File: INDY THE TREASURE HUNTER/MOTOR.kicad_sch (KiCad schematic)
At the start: 0 parts

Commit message: .
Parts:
- added M?: Motor_DC, symbol Motor:Motor_DC
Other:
- note added: "Driver"
- note added: "Motor"
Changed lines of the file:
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@@
 (kicad_sch (version 20230121) (generator eeschema)
   (paper "A4")
+  (rectangle (start 74.93 60.96) (end 105.41 90.17)
+    (stroke (width 0) (type default))
+    (fill (type none))
+  )
+  (rectangle (start 149.86 59.69) (end 196.85 95.25)
+    (stroke (width 0) (type default))
+    (fill (type none))
+  )
+  (text "Driver\n" (at 87.63 59.69 0)
+    (effects (font (size 1.27 1.27)) (justify left bottom))
+  )
+  (text "Motor\n" (at 168.91 57.15 0)
+    (effects (font (size 1.27 1.27)) (justify left bottom))
+  )
+  (symbol (lib_id "Motor:Motor_DC") (at 172.72 73.66 0) (unit 1)
+    (in_bom yes) (on_board yes) (dnp no) (fields_autoplaced)
+    (property "Reference" "M?" (at 177.8 75.565 0)
+      (effects (font (size 1.27 1.27)) (justify left))
+    )
+    (property "Value" "Motor_DC" (at 177.8 78.105 0)
+      (effects (font (size 1.27 1.27)) (justify left))
+    )
+    (property "Footprint" "" (at 172.72 75.946 0)
+      (effects (font (size 1.27 1.27)) hide)
+    )
+    (property "Datasheet" "~" (at 172.72 75.946 0)
+      (effects (font (size 1.27 1.27)) hide)
+    )
+    (pin "1")
+    (pin "2")
+    (instances
+      (project "INDY THE TREASURE HUNTER"
+        (path "/b3b90d4c-73f4-4a78-9e6e-dd19a1913646/0010784b-0c24-451a-8397-89ffe2babef6"
+          (reference "M?") (unit 1)
+        )
+      )
+    )
+  )
 )

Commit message: 17:32
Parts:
- gave numbers to parts that had none: 1
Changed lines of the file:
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@@
   (symbol (lib_id "Motor:Motor_DC") (at 172.72 73.66 0) (unit 1)
     (in_bom yes) (on_board yes) (dnp no) (fields_autoplaced)
-    (property "Reference" "M?" (at 177.8 75.565 0)
+    (property "Reference" "M1" (at 177.8 75.565 0)
       (effects (font (size 1.27 1.27)) (justify left))
     )
@@
       (project "INDY THE TREASURE HUNTER"
         (path "/b3b90d4c-73f4-4a78-9e6e-dd19a1913646/0010784b-0c24-451a-8397-89ffe2babef6"
-          (reference "M?") (unit 1)
+          (reference "M1") (unit 1)
         )
       )

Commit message: 23:43
Working on H-Bridge
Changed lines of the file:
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@@
 (kicad_sch (version 20230121) (generator eeschema)
   (paper "A4")
-  (rectangle (start 74.93 60.96) (end 105.41 90.17)
+  (rectangle (start 48.26 60.96) (end 114.3 125.73)
     (stroke (width 0) (type default))
     (fill (type none))
@@
     (fill (type none))
   )
-  (text "Driver\n" (at 87.63 59.69 0)
+  (text "Driver\n" (at 77.47 63.5 0)
     (effects (font (size 1.27 1.27)) (justify left bottom))
   )

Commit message: 00:53
Battery = done (?)
Motor control = done (no clue)
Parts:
- removed M1: Motor_DC, symbol Motor:Motor_DC
- added J4: Conn_01x11_Pin, symbol Connector:Conn_01x11_Pin
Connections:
- new net 12V: J4.1 (Pin_1)
- new net 5V: J4.3 (Pin_3)
- new net GND: J4.2 (Pin_2)
- new net MOT_CTRL_IN1: J4.4 (Pin_4)
- new net MOT_CTRL_IN2: J4.5 (Pin_5)
- new net MOT_CTRL_IN3: J4.8 (Pin_8)
- new net MOT_CTRL_IN4: J4.9 (Pin_9)
- new net OUT1: J4.6 (Pin_6)
- new net OUT2: J4.7 (Pin_7)
- new net OUT3: J4.10 (Pin_10)
- new net OUT4: J4.11 (Pin_11)
- no-connect marks 0 -> 1
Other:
- note added: "TODO: Confirm the wiring setup for the H-Bridge, really not totally sure about this I believe it goes: -5V to the 5V pin -GND is GND obviously -IN1 & IN2 (GPIO, 5V logic) drive OUT1 and OUT2 (To the motors) -Same with IN3 & IN4 -Need to find more detailed schematics -Mayyyyyyyybe leave 12V floating? Its not a logic port so"
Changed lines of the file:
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@@
 (kicad_sch (version 20230121) (generator eeschema)
   (paper "A4")
-  (rectangle (start 48.26 60.96) (end 114.3 125.73)
+  (no_connect (at 67.31 92.075))
+  (wire (pts (xy 60.96 112.395) (xy 72.39 112.395))
+    (stroke (width 0) (type default))
+  )
+  (wire (pts (xy 60.96 92.075) (xy 67.31 92.075))
+    (stroke (width 0) (type default))
+  )
+  (wire (pts (xy 60.96 107.315) (xy 67.31 107.315))
+    (stroke (width 0) (type default))
+  )
+  (wire (pts (xy 60.96 94.615) (xy 92.075 94.615))
+    (stroke (width 0) (type default))
+  )
+  (wire (pts (xy 60.96 109.855) (xy 72.39 109.855))
+    (stroke (width 0) (type default))
+  )
+  (wire (pts (xy 60.96 99.695) (xy 72.39 99.695))
+    (stroke (width 0) (type default))
+  )
+  (wire (pts (xy 60.96 97.155) (xy 72.39 97.155))
+    (stroke (width 0) (type default))
+  )
+  (wire (pts (xy 60.96 102.235) (xy 72.39 102.235))
+    (stroke (width 0) (type default))
+  )
+  (wire (pts (xy 60.96 117.475) (xy 67.31 117.475))
+    (stroke (width 0) (type default))
+  )
+  (wire (pts (xy 60.96 114.935) (xy 67.31 114.935))
+    (stroke (width 0) (type default))
+  )
+  (wire (pts (xy 92.075 94.615) (xy 92.075 96.52))
+    (stroke (width 0) (type default))
+  )
+  (wire (pts (xy 60.96 104.775) (xy 67.31 104.775))
+    (stroke (width 0) (type default))
+  )
+  (rectangle (start 48.26 60.96) (end 133.985 125.73)
     (stroke (width 0) (type default))
     (fill (type none))
@@
     (fill (type none))
   )
-  (text "Driver\n" (at 77.47 63.5 0)
+  (text "TODO: Confirm the wiring setup for the H-Bridge, really not totally sure about this\nI believe it goes:\n -5V to the 5V pin\n -GND is GND obviously\n -IN1 & IN2 (GPIO, 5V logic) drive OUT1 and OUT2 (To the motors)\n -Same with IN3 & IN4\n -Need to find more detailed schematics\n -Mayyyyyyyybe leave 12V floating? Its not a logic port so"
+    (at 49.784 80.01 0)
+    (effects (font (size 1.27 1.27)) (justify left bottom))
+  )
+  (text "Driver\n" (at 83.058 63.5 0)
     (effects (font (size 1.27 1.27)) (justify left bottom))
   )
@@
     (effects (font (size 1.27 1.27)) (justify left bottom))
   )
-  (symbol (lib_id "Motor:Motor_DC") (at 172.72 73.66 0) (unit 1)
+  (label "12V" (at 62.23 92.075 0) (fields_autoplaced)
+    (effects (font (size 1.27 1.27)) (justify left bottom))
+  )
+  (label "OUT4" (at 67.31 117.475 0) (fields_autoplaced)
+    (effects (font (size 1.27 1.27)) (justify left bottom))
+  )
+  (label "IN1" (at 67.31 99.695 0) (fields_autoplaced)
+    (effects (font (size 1.27 1.27)) (justify left bottom))
+  )
+  (label "OUT1" (at 67.31 104.775 0) (fields_autoplaced)
+    (effects (font (size 1.27 1.27)) (justify left bottom))
+  )
+  (label "GND" (at 67.31 94.615 0) (fields_autoplaced)
+    (effects (font (size 1.27 1.27)) (justify left bottom))
+  )
+  (label "OUT2" (at 67.31 107.315 0) (fields_autoplaced)
+    (effects (font (size 1.27 1.27)) (justify left bottom))
+  )
+  (label "IN2" (at 67.31 102.235 0) (fields_autoplaced)
+    (effects (font (size 1.27 1.27)) (justify left bottom))
+  )
+  (label "5V" (at 67.31 97.155 0) (fields_autoplaced)
+    (effects (font (size 1.27 1.27)) (justify left bottom))
+  )
+  (label "IN4" (at 67.31 112.395 0) (fields_autoplaced)
+    (effects (font (size 1.27 1.27)) (justify left bottom))
+  )
+  (label "IN3" (at 67.31 109.855 0) (fields_autoplaced)
+    (effects (font (size 1.27 1.27)) (justify left bottom))
+  )
+  (label "OUT3" (at 67.31 114.935 0) (fields_autoplaced)
+    (effects (font (size 1.27 1.27)) (justify left bottom))
+  )
+  (hierarchical_label "MOT_CTRL_IN2" (shape output) (at 72.39 102.235 0) (fields_autoplaced)
+    (effects (font (size 1.27 1.27)) (justify left))
+  )
+  (hierarchical_label "MOT_CTRL_IN4" (shape output) (at 72.39 112.395 0) (fields_autoplaced)
+    (effects (font (size 1.27 1.27)) (justify left))
+  )
+  (hierarchical_label "5V" (shape output) (at 72.39 97.155 0) (fields_autoplaced)
+    (effects (font (size 1.27 1.27)) (justify left))
+  )
+  (hierarchical_label "MOT_CTRL_IN3" (shape output) (at 72.39 109.855 0) (fields_autoplaced)
+    (effects (font (size 1.27 1.27)) (justify left))
+  )
+  (hierarchical_label "MOT_CTRL_IN1" (shape output) (at 72.39 99.695 0) (fields_autoplaced)
+    (effects (font (size 1.27 1.27)) (justify left))
+  )
+  (symbol (lib_id "power:GND") (at 92.075 96.52 0) (unit 1)
     (in_bom yes) (on_board yes) (dnp no) (fields_autoplaced)
-    (property "Reference" "M1" (at 177.8 75.565 0)
-      (effects (font (size 1.27 1.27)) (justify left))
-    )
-    (property "Value" "Motor_DC" (at 177.8 78.105 0)
-      (effects (font (size 1.27 1.27)) (justify left))
-    )
-    (property "Footprint" "" (at 172.72 75.946 0)
+    (property "Reference" "#PWR013" (at 92.075 102.87 0)
       (effects (font (size 1.27 1.27)) hide)
     )
-    (property "Datasheet" "~" (at 172.72 75.946 0)
+    (property "Value" "GND" (at 92.075 100.838 0)
+      (effects (font (size 1.27 1.27)))
+    )
+    (property "Footprint" "" (at 92.075 96.52 0)
+      (effects (font (size 1.27 1.27)) hide)
+    )
+    (property "Datasheet" "" (at 92.075 96.52 0)
       (effects (font (size 1.27 1.27)) hide)
     )
     (pin "1")
-    (pin "2")
     (instances
       (project "INDY THE TREASURE HUNTER"
         (path "/b3b90d4c-73f4-4a78-9e6e-dd19a1913646/0010784b-0c24-451a-8397-89ffe2babef6"
-          (reference "M1") (unit 1)
+          (reference "#PWR013") (unit 1)
         )
       )
+    )
+  )
+  (symbol (lib_id "Connector:Conn_01x11_Pin") (at 55.88 104.775 0) (unit 1)
+    (in_bom yes) (on_board yes) (dnp yes) (fields_autoplaced)
+    (property "Reference" "J4" (at 56.515 86.995 0)
+      (effects (font (size 1.27 1.27)))
+    )
+    (property "Value" "Conn_01x11_Pin" (at 56.515 89.535 0)
+      (effects (font (size 1.27 1.27)))
+    )
+    (property "Footprint" "" (at 55.88 104.775 0)
+      (effects (font (size 1.27 1.27)) hide)
+    )
+    (property "Datasheet" "~" (at 55.88 104.775 0)
+      (effects (font (size 1.27 1.27)) hide)
+    )
+    (pin "1")
+    (pin "10")
+    (pin "11")
+    (pin "2")
+    (pin "3")
+    (pin "4")
+    (pin "5")
+    (pin "6")
+    (pin "7")
+    (pin "8")
+    (pin "9")
+    (instances
+      (project "INDY THE TREASURE HUNTER"
+        (path "/b3b90d4c-73f4-4a78-9e6e-dd19a1913646/0010784b-0c24-451a-8397-89ffe2babef6"
+          (reference "J4") (unit 1)
+        )
+      )

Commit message: I think thats that?
There are a few things that remain unclear. For milestone 1's handin, it should be ok, just some cleanup in the morning might be necessary and group discussion on how to do things
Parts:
- added M1, M2: Motor_DC, symbol Motor:Motor_DC
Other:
- note added: "Not sure how to hook these up without being sure about the H-bridge."
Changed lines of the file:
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@@
+    (effects (font (size 1.27 1.27)) (justify left bottom))
+  )
+  (text "Not sure how to hook these up without being sure about the\nH-bridge."
+    (at 199.39 67.31 0)
     (effects (font (size 1.27 1.27)) (justify left bottom))
   )
@@
     )
   )
+  (symbol (lib_id "Motor:Motor_DC") (at 182.245 76.835 0) (unit 1)
+    (in_bom yes) (on_board yes) (dnp no) (fields_autoplaced)
+    (property "Reference" "M2" (at 186.69 78.105 0)
+      (effects (font (size 1.27 1.27)) (justify left))
+    )
+    (property "Value" "Motor_DC" (at 186.69 80.645 0)
+      (effects (font (size 1.27 1.27)) (justify left))
+    )
+    (property "Footprint" "" (at 182.245 79.121 0)
+      (effects (font (size 1.27 1.27)) hide)
+    )
+    (property "Datasheet" "~" (at 182.245 79.121 0)
+      (effects (font (size 1.27 1.27)) hide)
+    )
+    (pin "1")
+    (pin "2")
+    (instances
+      (project "INDY THE TREASURE HUNTER"
+        (path "/b3b90d4c-73f4-4a78-9e6e-dd19a1913646/0010784b-0c24-451a-8397-89ffe2babef6"
+          (reference "M2") (unit 1)
+        )
+      )
+    )
+  )
   (symbol (lib_id "Connector:Conn_01x11_Pin") (at 55.88 104.775 0) (unit 1)
     (in_bom yes) (on_board yes) (dnp yes) (fields_autoplaced)
@@
         )
       )
+    )
+  )
+  (symbol (lib_id "Motor:Motor_DC") (at 159.385 76.835 0) (unit 1)
+    (in_bom yes) (on_board yes) (dnp no) (fields_autoplaced)
+    (property "Reference" "M1" (at 163.83 78.105 0)
+      (effects (font (size 1.27 1.27)) (justify left))
+    )
+    (property "Value" "Motor_DC" (at 163.83 80.645 0)
+      (effects (font (size 1.27 1.27)) (justify left))
+    )
+    (property "Footprint" "" (at 159.385 79.121 0)
+      (effects (font (size 1.27 1.27)) hide)
+    )
+    (property "Datasheet" "~" (at 159.385 79.121 0)
+      (effects (font (size 1.27 1.27)) hide)
+    )
+    (pin "1")
+    (pin "2")
+    (instances
+      (project "INDY THE TREASURE HUNTER"
+        (path "/b3b90d4c-73f4-4a78-9e6e-dd19a1913646/0010784b-0c24-451a-8397-89ffe2babef6"
+          (reference "M1") (unit 1)
+        )
+      )

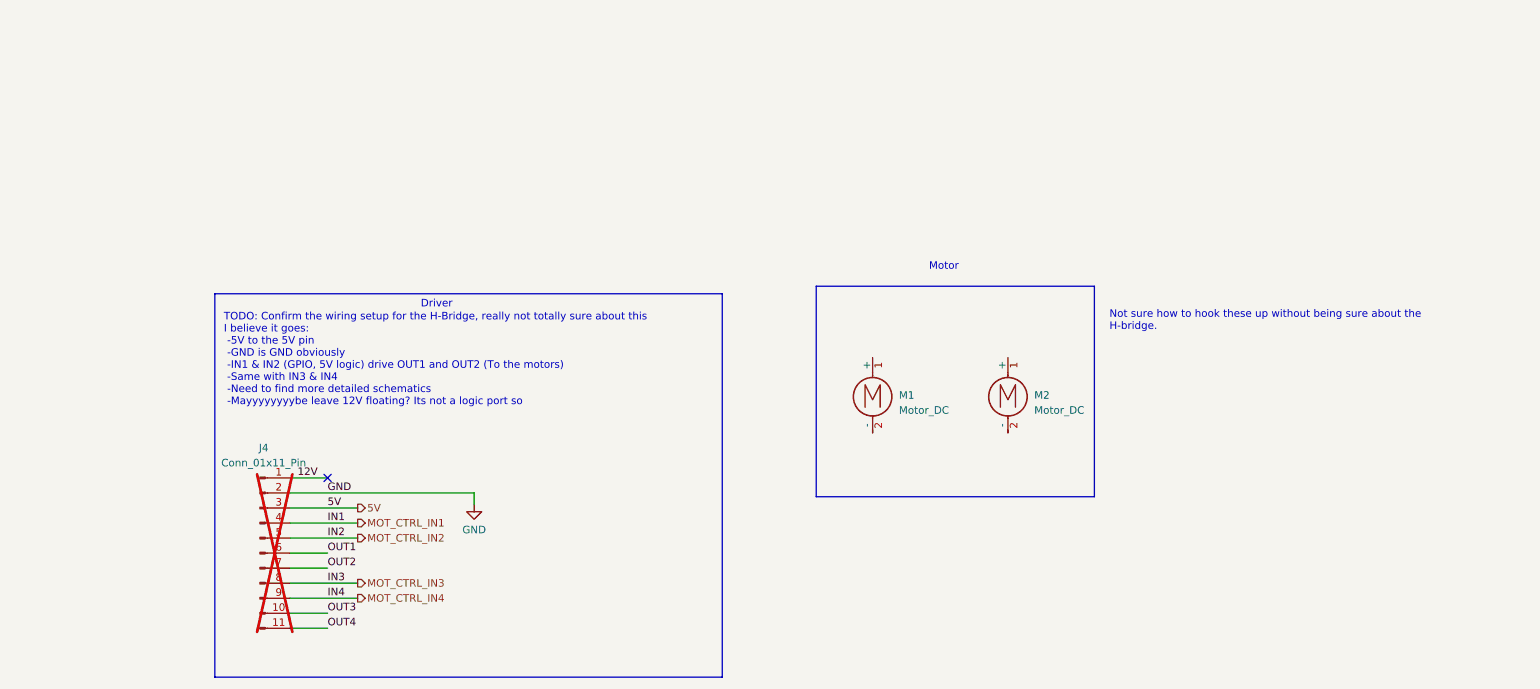
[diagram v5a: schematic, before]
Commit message: Neatened up schematic for milestone 1 handin
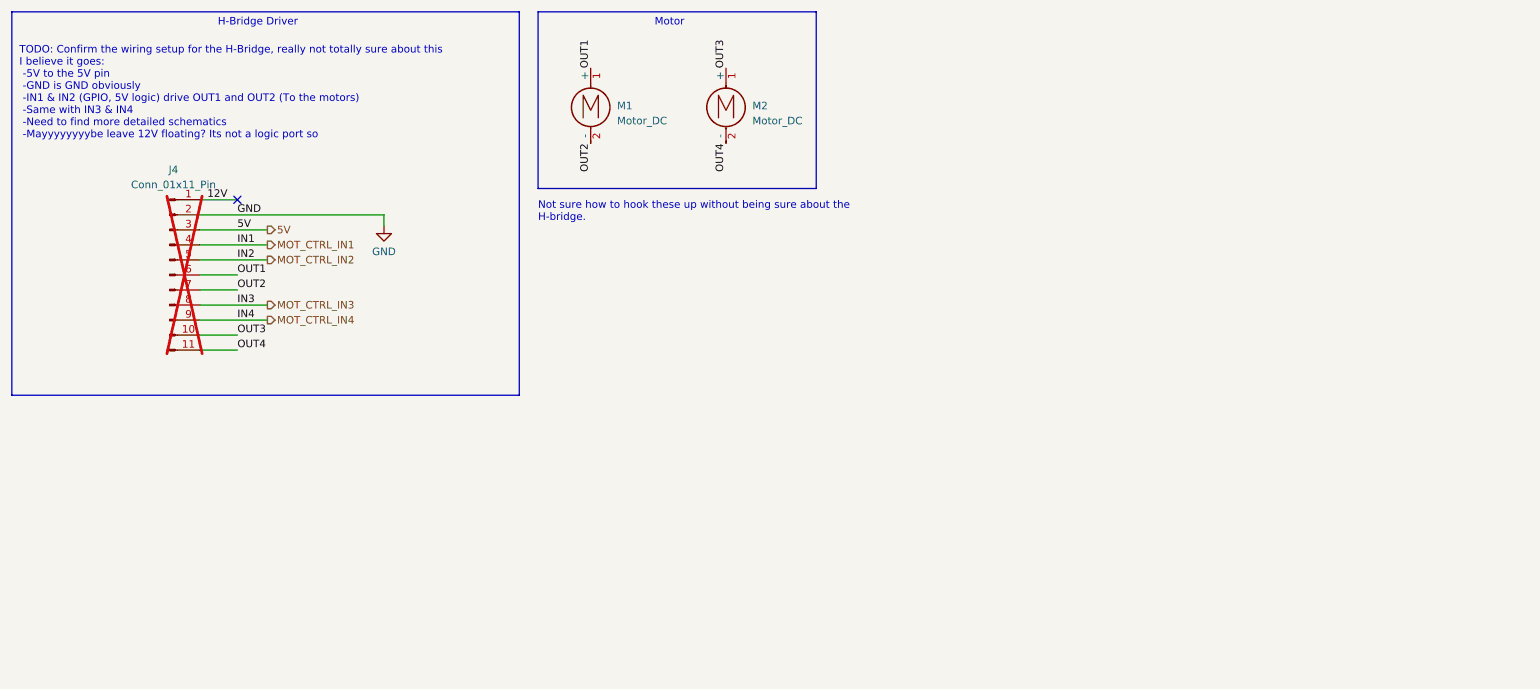
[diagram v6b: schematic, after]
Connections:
- net OUT1: now also M1.1 (+)
- net OUT2: now also M1.2 (-)
- net OUT3: now also M2.1 (+)
- net OUT4: now also M2.2 (-)
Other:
- note added: "H-Bridge Driver"
- note removed: "Driver"
- moved on the sheet: J4, M1, M2
